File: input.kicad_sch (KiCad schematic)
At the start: 6 parts, among them U7 4N35

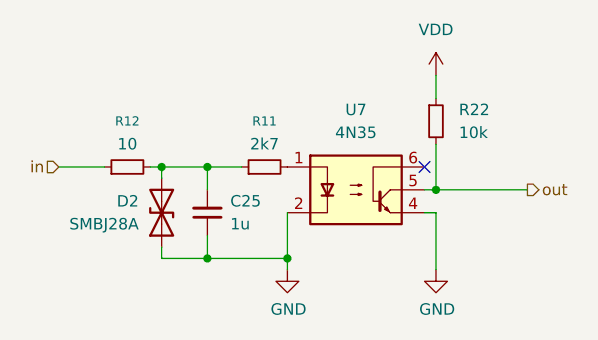
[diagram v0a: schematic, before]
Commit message: Finish rev0 schematics.
Signed-off-by: Dominik Bayerl <dominik.bayerl@carissma.eu>
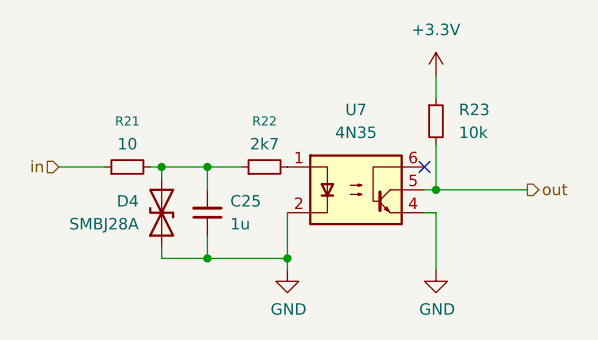
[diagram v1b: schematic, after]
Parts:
- C25: footprint (none) -> Capacitor_SMD:C_0603_1608Metric_Pad1.08x0.95mm_HandSolder
- D4: renamed from D2; footprint (none) -> Diode_SMD:D_SMA_Handsoldering
- renumbered R12 to R21, R11 to R22, R22 to R23
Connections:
- net VDD renamed +3.3V

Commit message: Assign footprints.
Signed-off-by: Dominik Bayerl <dominik.bayerl@carissma.eu>
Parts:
- R21, R22: footprint (none) -> Resistor_SMD:R_0603_1608Metric_Pad0.98x0.95mm_HandSolder
- R23: footprint Resistor_SMD:R_1206_3216Metric -> Resistor_SMD:R_0603_1608Metric_Pad0.98x0.95mm_HandSolder
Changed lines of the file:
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@@
 			)
 		)
-		(property "Footprint" "Resistor_SMD:R_1206_3216Metric"
+		(property "Footprint" "Resistor_SMD:R_0603_1608Metric_Pad0.98x0.95mm_HandSolder"
 			(at 166.37 93.98 0)
 			(effects
@@
 			)
 		)
-		(property "Footprint" ""
+		(property "Footprint" "Resistor_SMD:R_0603_1608Metric_Pad0.98x0.95mm_HandSolder"
 			(at 147.32 99.06 0)
 			(effects
@@
 			)
 		)
-		(property "Footprint" ""
+		(property "Footprint" "Resistor_SMD:R_0603_1608Metric_Pad0.98x0.95mm_HandSolder"
 			(at 132.08 99.06 0)
 			(effects
